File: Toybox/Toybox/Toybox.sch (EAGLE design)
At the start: 28 parts, among them J2 RASPBERRYPI-40-PIN-GPIO, X1 USB-A-TH

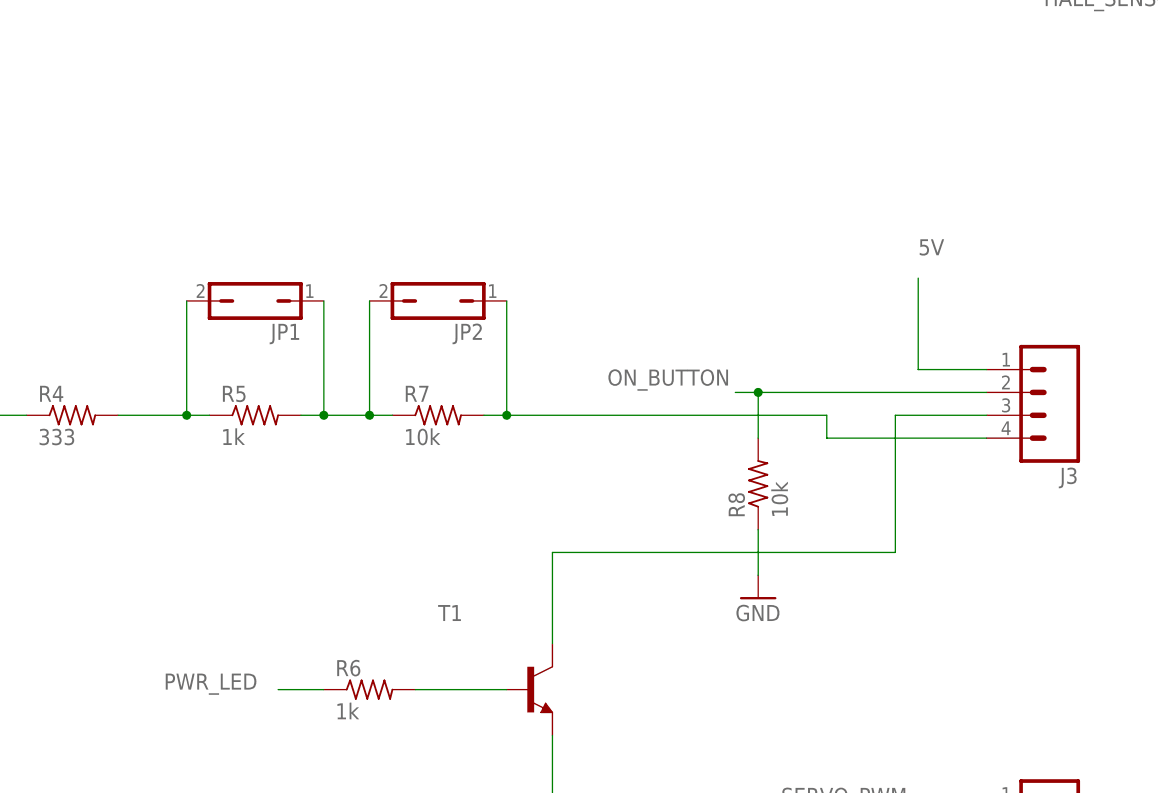
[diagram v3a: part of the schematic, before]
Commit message: Removing the ignored files. Started personal DRU and CAM folder. Created BOM
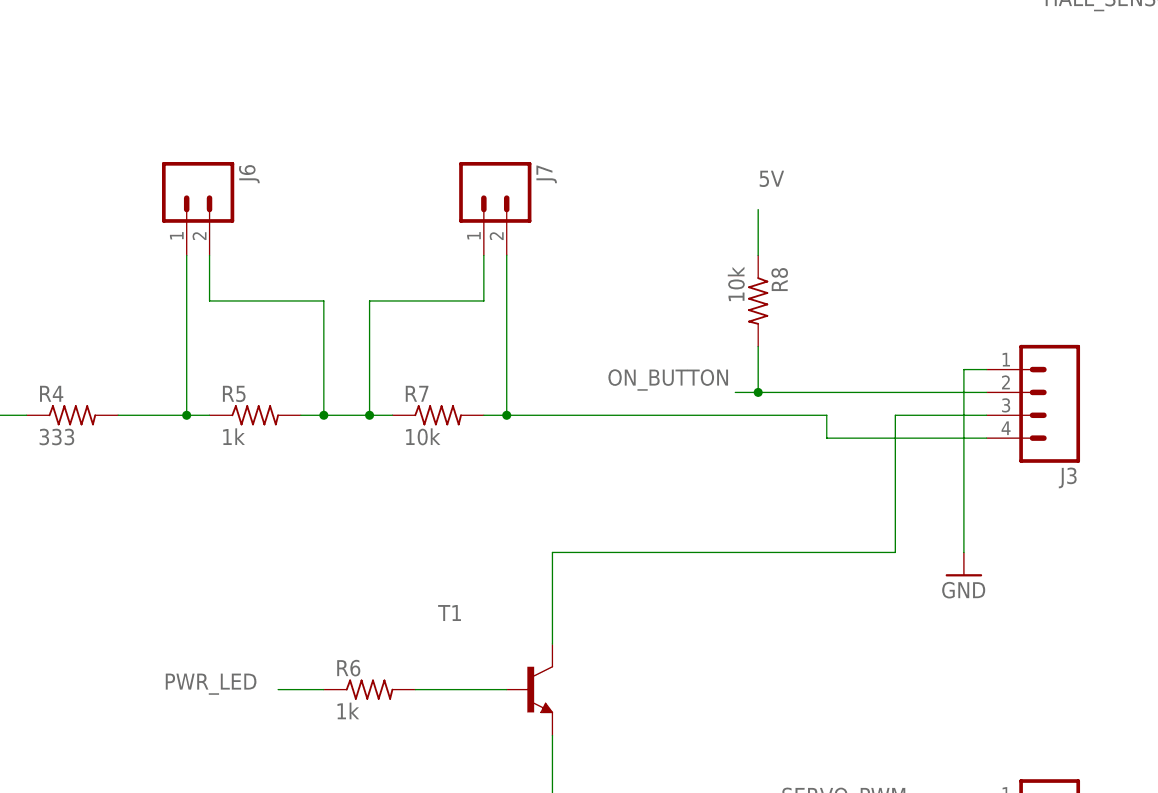
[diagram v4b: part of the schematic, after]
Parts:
- removed JP1, JP2: (no value), jumper:JP1Q
- added J6, J7: (no value), SparkFun-Connectors:M02PTH
- J3: device SparkFun-Connectors:M04PTH -> SparkFun-Connectors:M041X04_NO_SILK
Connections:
- net 5V: now also R8.1; no longer J3.1
- net GND: now also J3.1; no longer R8.1
- net N$7: now also J6.1; no longer JP1.2
- net N$8: now also J6.2, J7.1; no longer JP1.1, JP2.2
- net N$9: now also J7.2; no longer JP2.1
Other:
- moved on the sheet: R8
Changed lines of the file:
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@@
 <part name="GND11" library="supply1" deviceset="GND" device=""/>
 <part name="R8" library="resistor" deviceset="R-US_" device="R0603" value="10k"/>
-<part name="GND9" library="supply1" deviceset="GND" device=""/>
 <part name="GND10" library="supply1" deviceset="GND" device=""/>
 <part name="T1" library="transistor" deviceset="*-NPN-" device="SOT23-BEC" technology="MMBT2222ALT1"/>
@@
 <part name="R5" library="resistor" deviceset="R-US_" device="R0603" value="1k"/>
 <part name="R4" library="resistor" deviceset="R-US_" device="R0603" value="333"/>
-<part name="JP2" library="jumper" deviceset="JP1Q" device=""/>
-<part name="JP1" library="jumper" deviceset="JP1Q" device=""/>
 <part name="J1" library="SparkFun-Connectors" deviceset="M02" device="5MM"/>
 <part name="L1" library="Toybox" deviceset="SRN1060" device="" value="10uH"/>
-<part name="J3" library="SparkFun-Connectors" deviceset="M04" device="PTH"/>
+<part name="J3" library="SparkFun-Connectors" deviceset="M04" device="1X04_NO_SILK"/>
 <part name="J4" library="SparkFun-Connectors" deviceset="M03" device="PTH"/>
 <part name="J5" library="SparkFun-Connectors" deviceset="M03" device="PTH"/>
+<part name="J6" library="SparkFun-Connectors" deviceset="M02" device="PTH"/>
+<part name="J7" library="SparkFun-Connectors" deviceset="M02" device="PTH"/>
+<part name="GND9" library="supply1" deviceset="GND" device=""/>
 </parts>
 <sheets>
@@
 </instance>
 <instance part="GND11" gate="1" x="289.56" y="83.82"/>
-<instance part="R8" gate="G$1" x="220.98" y="53.34" rot="R90"/>
-<instance part="GND9" gate="1" x="220.98" y="40.64"/>
+<instance part="R8" gate="G$1" x="220.98" y="73.66" rot="R270"/>
 <instance part="GND10" gate="1" x="238.76" y="2.54"/>
 <instance part="T1" gate="G$1" x="195.58" y="30.48"/>
@@
 <instance part="R5" gate="G$1" x="165.1" y="60.96"/>
 <instance part="R4" gate="G$1" x="144.78" y="60.96"/>
-<instance part="JP2" gate="A" x="185.42" y="73.66" rot="R90"/>
-<instance part="JP1" gate="A" x="165.1" y="73.66" rot="R90"/>
 <instance part="J1" gate="G$1" x="2.54" y="154.94" rot="MR180"/>
 <instance part="L1" gate="G$1" x="104.14" y="147.32" smashed="yes">
@@
 <instance part="J4" gate="J$1" x="254" y="15.24" rot="R180"/>
 <instance part="J5" gate="J$1" x="309.88" y="106.68" rot="R180"/>
+<instance part="J6" gate="G$1" x="157.48" y="86.36" rot="R270"/>
+<instance part="J7" gate="G$1" x="190.5" y="86.36" rot="R270"/>
+<instance part="GND9" gate="1" x="243.84" y="43.18"/>
 </instances>
 <busses>
@@
 </segment>
 <segment>
-<pinref part="GND9" gate="1" pin="GND"/>
-<pinref part="R8" gate="G$1" pin="1"/>
-<wire x1="220.98" y1="48.26" x2="220.98" y2="43.18" width="0.1524" layer="91"/>
-</segment>
-<segment>
 <wire x1="246.38" y1="12.7" x2="238.76" y2="12.7" width="0.1524" layer="91"/>
 <wire x1="238.76" y1="12.7" x2="238.76" y2="5.08" width="0.1524" layer="91"/>
@@
 <wire x1="297.18" y1="104.14" x2="297.18" y2="91.44" width="0.1524" layer="91"/>
 <wire x1="297.18" y1="91.44" x2="289.56" y2="91.44" width="0.1524" layer="91"/>
+</segment>
+<segment>
+<pinref part="J3" gate="G$1" pin="1"/>
+<wire x1="246.38" y1="66.04" x2="243.84" y2="66.04" width="0.1524" layer="91"/>
+<wire x1="243.84" y1="66.04" x2="243.84" y2="45.72" width="0.1524" layer="91"/>
+<pinref part="GND9" gate="1" pin="GND"/>
 </segment>
 </net>
@@
 </segment>
 <segment>
-<wire x1="246.38" y1="66.04" x2="238.76" y2="66.04" width="0.1524" layer="91"/>
-<wire x1="238.76" y1="66.04" x2="238.76" y2="76.2" width="0.1524" layer="91"/>
-<label x="238.76" y="78.74" size="1.778" layer="95"/>
-<pinref part="J3" gate="G$1" pin="1"/>
-</segment>
-<segment>
 <wire x1="246.38" y1="15.24" x2="238.76" y2="15.24" width="0.1524" layer="91"/>
 <label x="235.204" y="14.986" size="1.778" layer="95"/>
 <pinref part="J4" gate="J$1" pin="2"/>
+</segment>
+<segment>
+<pinref part="R8" gate="G$1" pin="1"/>
+<wire x1="220.98" y1="78.74" x2="220.98" y2="83.82" width="0.1524" layer="91"/>
+<label x="220.98" y="86.36" size="1.778" layer="95"/>
 </segment>
 </net>
@@
 <pinref part="R8" gate="G$1" pin="2"/>
 <wire x1="220.98" y1="63.5" x2="218.44" y2="63.5" width="0.1524" layer="91"/>
-<wire x1="220.98" y1="58.42" x2="220.98" y2="63.5" width="0.1524" layer="91"/>
+<wire x1="220.98" y1="68.58" x2="220.98" y2="63.5" width="0.1524" layer="91"/>
 <junction x="220.98" y="63.5"/>
 <label x="204.216" y="64.262" size="1.778" layer="95"/>
@@
 <pinref part="R4" gate="G$1" pin="2"/>
 <pinref part="R5" gate="G$1" pin="1"/>
-<pinref part="JP1" gate="A" pin="2"/>
 <wire x1="149.86" y1="60.96" x2="157.48" y2="60.96" width="0.1524" layer="91"/>
 <wire x1="157.48" y1="60.96" x2="160.02" y2="60.96" width="0.1524" layer="91"/>
-<wire x1="157.48" y1="73.66" x2="157.48" y2="60.96" width="0.1524" layer="91"/>
+<wire x1="157.48" y1="78.74" x2="157.48" y2="60.96" width="0.1524" layer="91"/>
 <junction x="157.48" y="60.96"/>
+<pinref part="J6" gate="G$1" pin="1"/>
 </segment>
 </net>
@@
 <pinref part="R7" gate="G$1" pin="1"/>
 <wire x1="170.18" y1="60.96" x2="172.72" y2="60.96" width="0.1524" layer="91"/>
-<pinref part="JP2" gate="A" pin="2"/>
 <wire x1="172.72" y1="60.96" x2="177.8" y2="60.96" width="0.1524" layer="91"/>
 <wire x1="177.8" y1="60.96" x2="180.34" y2="60.96" width="0.1524" layer="91"/>
 <wire x1="177.8" y1="73.66" x2="177.8" y2="60.96" width="0.1524" layer="91"/>
 <junction x="177.8" y="60.96"/>
-<pinref part="JP1" gate="A" pin="1"/>
 <wire x1="172.72" y1="73.66" x2="172.72" y2="60.96" width="0.1524" layer="91"/>
 <junction x="172.72" y="60.96"/>
+<pinref part="J6" gate="G$1" pin="2"/>
+<wire x1="160.02" y1="78.74" x2="160.02" y2="73.66" width="0.1524" layer="91"/>
+<wire x1="160.02" y1="73.66" x2="172.72" y2="73.66" width="0.1524" layer="91"/>
+<pinref part="J7" gate="G$1" pin="1"/>
+<wire x1="177.8" y1="73.66" x2="190.5" y2="73.66" width="0.1524" layer="91"/>
+<wire x1="190.5" y1="73.66" x2="190.5" y2="78.74" width="0.1524" layer="91"/>
 </segment>
 </net>
@@
 <pinref part="R7" gate="G$1" pin="2"/>
 <wire x1="190.5" y1="60.96" x2="193.04" y2="60.96" width="0.1524" layer="91"/>
-<pinref part="JP2" gate="A" pin="1"/>
-<wire x1="193.04" y1="73.66" x2="193.04" y2="60.96" width="0.1524" layer="91"/>
+<wire x1="193.04" y1="78.74" x2="193.04" y2="60.96" width="0.1524" layer="91"/>
 <pinref part="J3" gate="G$1" pin="4"/>
 <wire x1="246.38" y1="58.42" x2="228.6" y2="58.42" width="0.1524" layer="91"/>
@@
 <wire x1="228.6" y1="60.96" x2="193.04" y2="60.96" width="0.1524" layer="91"/>
 <junction x="193.04" y="60.96"/>
-</segment>
-</net>
+<pinref part="J7" gate="G$1" pin="2"/>
+</segment>
+</net>

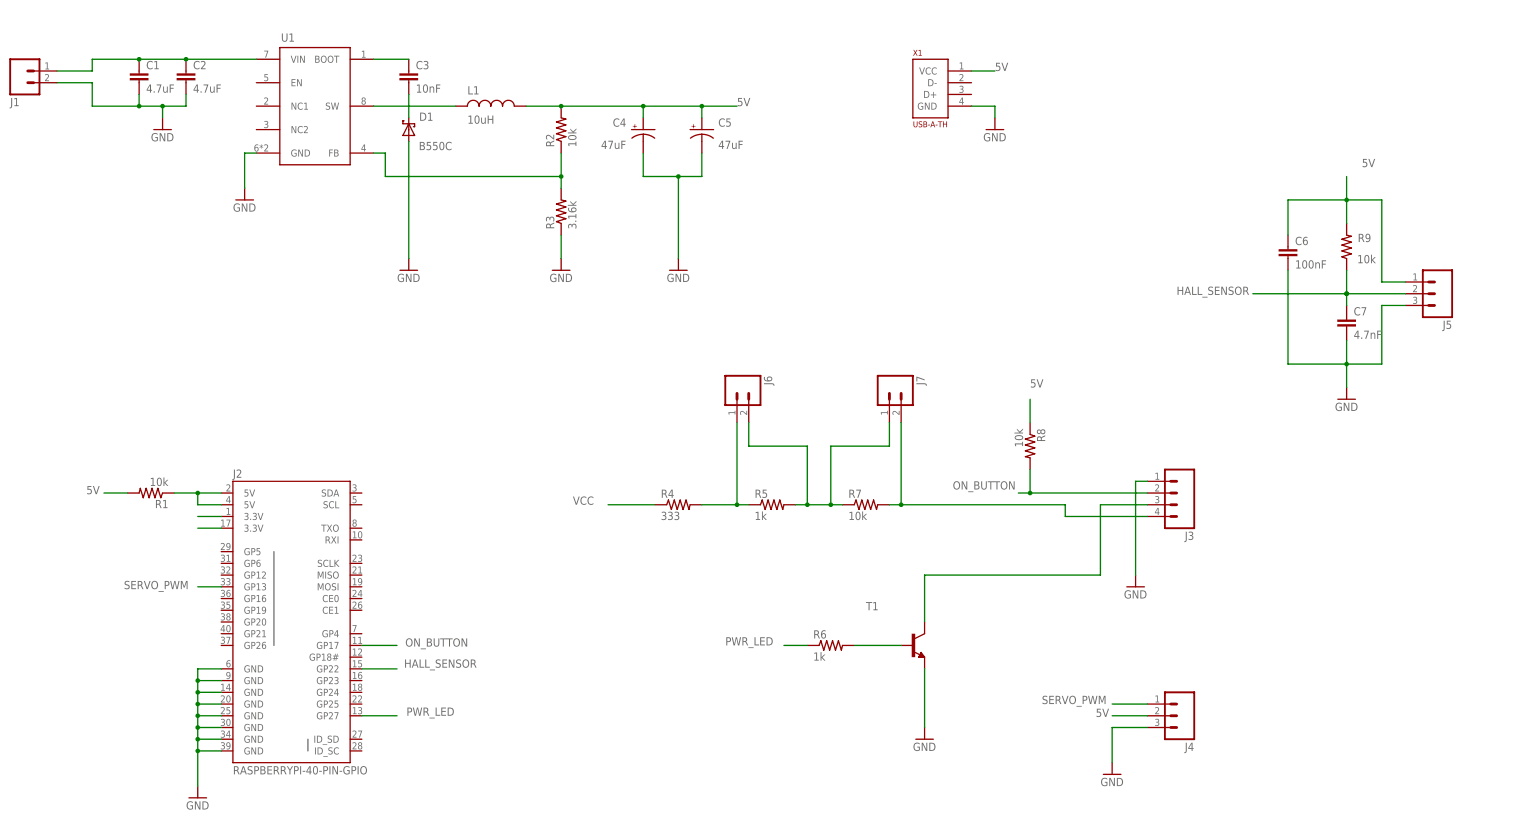
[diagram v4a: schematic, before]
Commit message: Fixed up the toybox board. Added different passive components all around
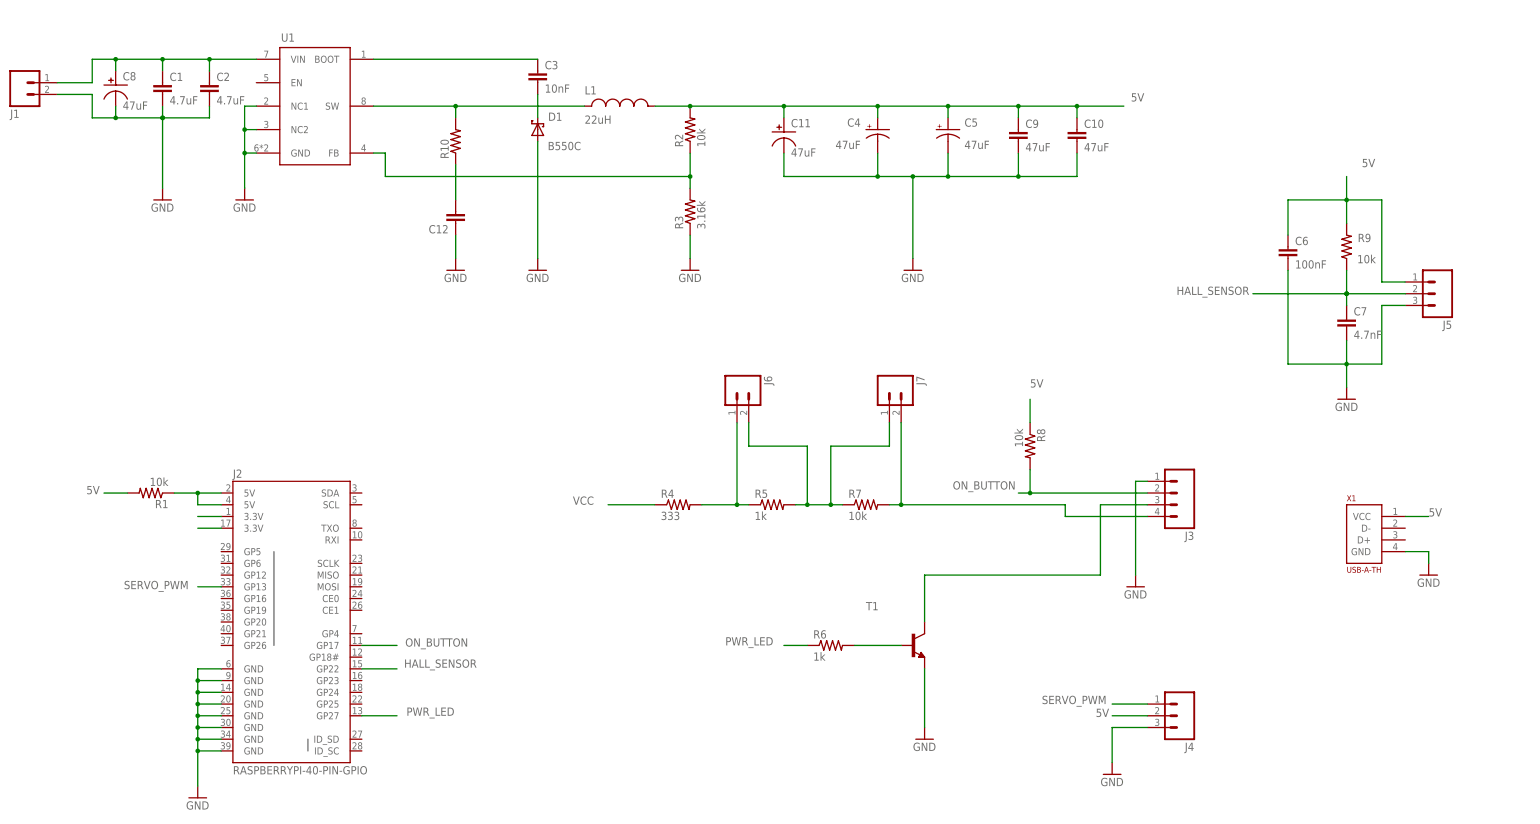
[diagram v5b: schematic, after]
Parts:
- added C10, C9: 47uF, SparkFun-Passives:CAP1210
- added C11: 47uF, Master:CPOL-SVPF-6.3
- added C12: (no value), resistor:C-EUC0805
- added C8: 47uF, Master:CPOL-UUR-6.3
- added R10: (no value), resistor:R-US_R0805
- C3, C6, C7: device resistor:C-EUC0603 -> resistor:C-EUC0805
- L1: value 10uH -> 22uH; device Toybox:SRN1060 -> Master:SRR1210
- R1, R2, R3, R4, R5, R6, R7, R8, R9: device resistor:R-US_R0603 -> resistor:R-US_R0805
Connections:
- new net N$10: C12.2, R10.1
- net 5V: now also C10.1, C11.P$1, C9.1, L1.P$2; no longer L1.2
- net GND: now also C10.2, C11.P$2, C12.1, C8.P$2, C9.2, U1.NC1, U1.NC2
- net SW: now also L1.P$1, R10.2; no longer L1.1
- net VCC: now also C8.P$1
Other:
- moved on the sheet: C1, C2, C3, C4, C5, D1, J1, L1, R2, R3, X1
